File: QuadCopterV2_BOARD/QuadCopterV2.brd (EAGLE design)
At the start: 100 x 80 mm, 10 parts, among them IC1 EK-TM4C123GXLP, U1 GY-63MS5611, U2 GY-521MPU6050, U3 GY-63MS5611

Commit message: Eagle board design in process
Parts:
- removed U$1: SIM800L, SIM800L:SIP
- added U$7: SIM800L, SIM800L:SIP
- moved U1 277.7 mm to (-95.2, -166.4)
- moved U2 269.4 mm to (-95.2, -186.7)
- moved U$6 268.1 mm to (-85.1, -210.8)
- moved U$5 229.5 mm to (-104.1, -129.5)
- moved U3 228.9 mm to (-91.4, -143.5)
- moved U$3 196.5 mm to (-83.8, -105.4)
- moved U$2 162.0 mm to (-94.0, -39.4)
- moved U$4 113.8 mm to (-92.7, -71.1)
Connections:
- removed net N$27: U$1.3
- removed net N$28: U$1.4
- removed net N$30: U$1.7
- removed net N$31: U$1.5
- new net 5V1: U$2.D2
- new net N$1: U$7.3
- new net N$15: U$7.5
- new net N$6: U$7.4
- new net N$7: U$7.7
- net 5V0: now also U$7.1; no longer U$1.1, U$2.D2
- net GND: now also U$7.2, U$7.6; no longer U$1.2, U$1.6

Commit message: added modifications to eagle board, and to the mpu-6050 code
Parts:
- moved U$6 300.0 mm to (89.4, 33.2), turned to 90 degrees
- moved U2 293.4 mm to (36.8, 75.3), turned to 90 degrees
- moved U1 291.3 mm to (67.3, 75.3), turned to 90 degrees
- moved U$7 247.4 mm to (104.5, 103.0), turned to 225 degrees
- moved U$5 238.5 mm to (21.2, 73.3), turned to 135 degrees
- moved U3 217.6 mm to (74.1, -2.29), turned to 180 degrees
- moved U$2 197.2 mm to (101.5, -13.3), turned to 315 degrees
- moved U$3 162.7 mm to (1.19, 33.3), turned to 90 degrees
- moved IC1 132.9 mm to (51.5, 18.7)
- moved U$4 121.1 mm to (11.5, -9.49), turned to 135 degrees
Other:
- board size 100 x 80 mm -> 107.8 x 108.1 mm

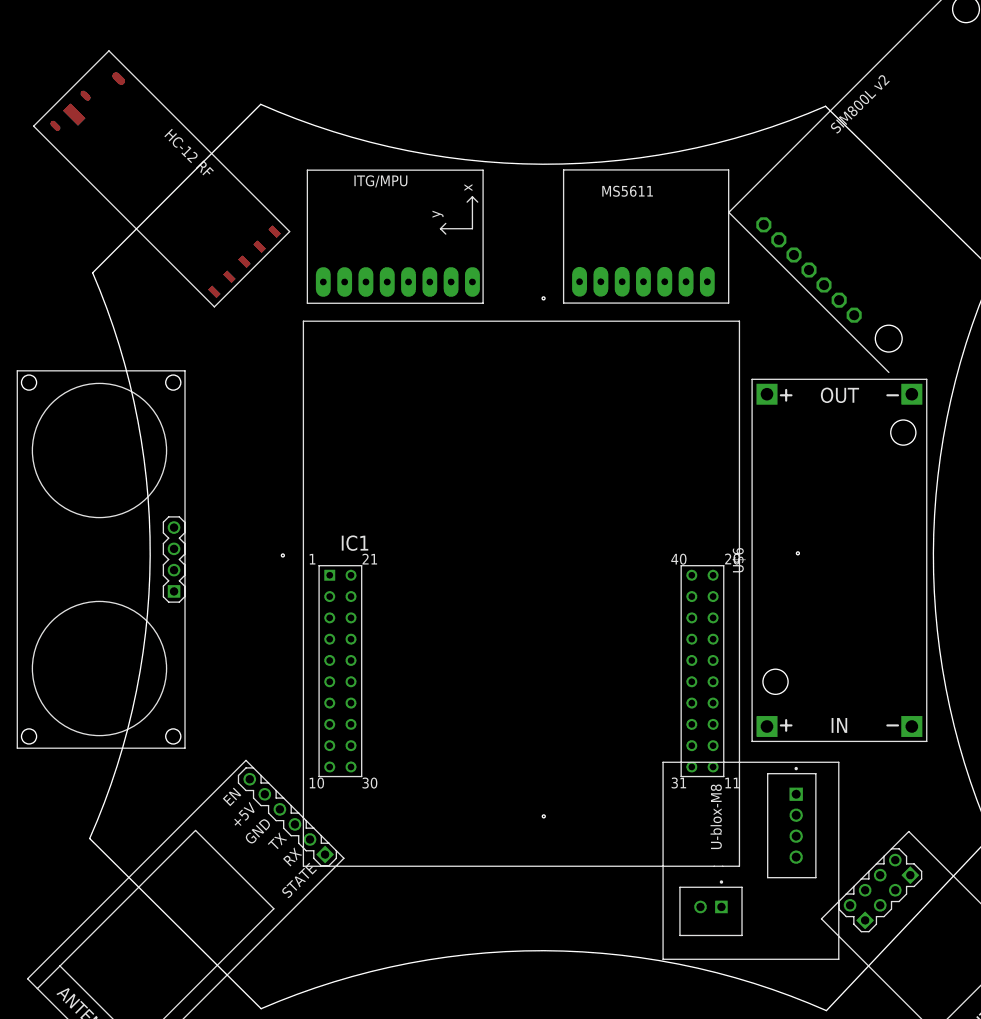
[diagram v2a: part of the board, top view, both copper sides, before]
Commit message: mpu-6050 finished, added more board eagle files, added altimeter code
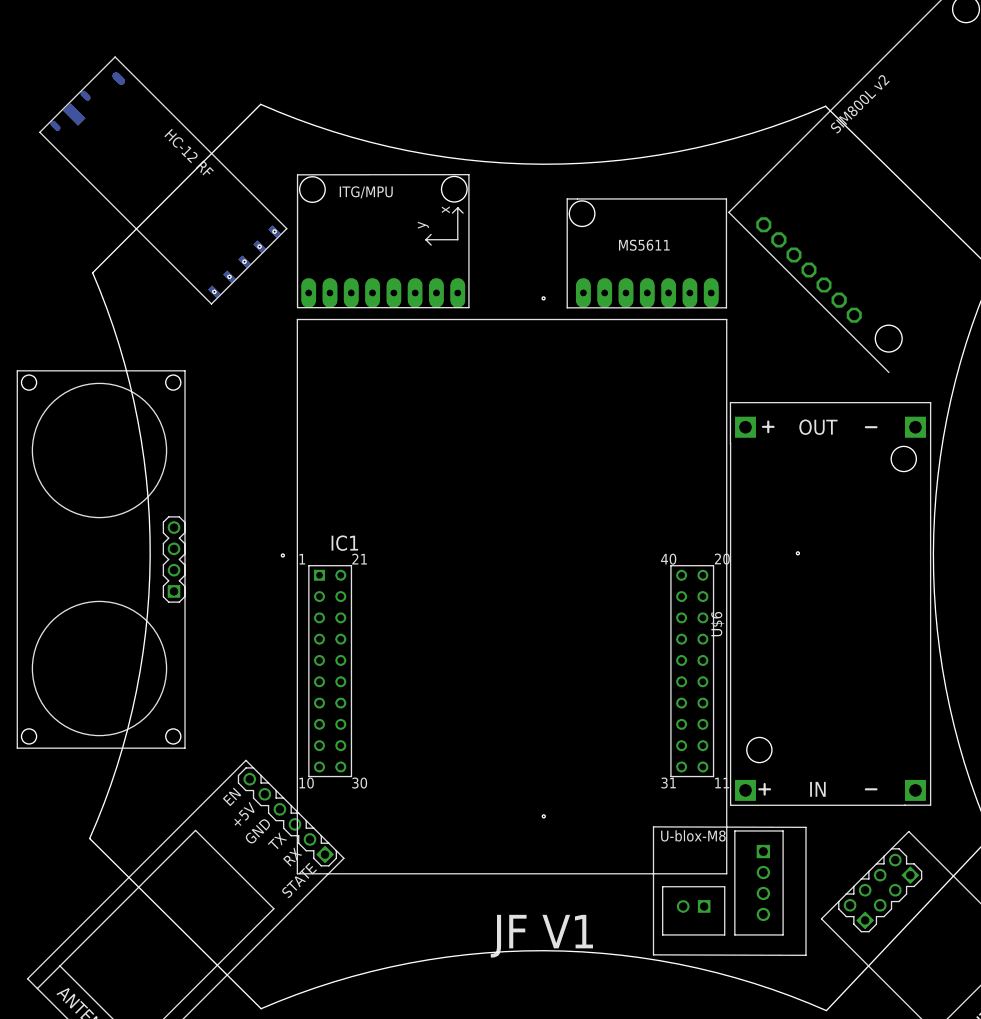
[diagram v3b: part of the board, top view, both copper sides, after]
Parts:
- moved U$6 8.04 mm to (86.9, 25.6)
- moved U3 7.87 mm to (70.2, -9.12)
- moved U2 2.18 mm to (35.0, 74.0)
- moved U1 1.41 mm to (67.8, 74.0)
- moved IC1 1.22 mm to (50.3, 18.7)
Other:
- board text added: "JF V1"
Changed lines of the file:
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@@
 <setting verticaltext="up"/>
 </settings>
-<grid distance="1" unitdist="mil" unit="mil" style="lines" multiple="1" display="no" altdistance="5" altunitdist="mil" altunit="mil"/>
+<grid distance="0.001" unitdist="mm" unit="mm" style="lines" multiple="1" display="no" altdistance="5" altunitdist="mil" altunit="mil"/>
 <layers>
 <layer number="1" name="Top" color="4" fill="1" visible="yes" active="yes"/>
@@
 <hole x="23.0632" y="33.8074" drill="0.35"/>
 <hole x="84.4804" y="34.0614" drill="0.35"/>
+<text x="54.306" y="-11.048" size="4" layer="21" font="fixed" align="center">JF V1</text>
 </plain>
 <attributes>
@@
 </autorouter>
 <elements>
-<element name="IC1" library="EK-TM4C123GXL" package="TM4C123LAUNCHPAD" value="EK-TM4C123GXLP" x="51.5112" y="18.7452" smashed="yes">
-<attribute name="AVAILABILITY" value="Unavailable" x="132.7912" y="4.7752" size="1.778" layer="27" display="off"/>
-<attribute name="DESCRIPTION" value=" TM4C123G LaunchPad™ Tiva™ C ARM® Cortex®-M4F MCU 32-Bit Embedded Evaluation Board " x="132.7912" y="4.7752" size="1.778" layer="27" display="off"/>
-<attribute name="MF" value="Texas Instruments" x="132.7912" y="4.7752" size="1.778" layer="27" display="off"/>
-<attribute name="MP" value="EK-TM4C123GXL" x="132.7912" y="4.7752" size="1.778" layer="27" display="off"/>
-<attribute name="NAME" x="33.4534" y="36.1671" size="1.780340625" layer="25" ratio="10" rot="R180"/>
-<attribute name="PACKAGE" value="None" x="132.7912" y="4.7752" size="1.778" layer="27" display="off"/>
-<attribute name="PRICE" value="None" x="132.7912" y="4.7752" size="1.778" layer="27" display="off"/>
-<attribute name="VALUE" x="69.3157" y="34.3114" size="1.78045" layer="27" ratio="10"/>
+<element name="IC1" library="EK-TM4C123GXL" package="TM4C123LAUNCHPAD" value="EK-TM4C123GXLP" x="50.292" y="18.7452" smashed="yes">
+<attribute name="AVAILABILITY" value="Unavailable" x="131.572" y="4.7752" size="1.778" layer="27" display="off"/>
+<attribute name="DESCRIPTION" value=" TM4C123G LaunchPad™ Tiva™ C ARM® Cortex®-M4F MCU 32-Bit Embedded Evaluation Board " x="131.572" y="4.7752" size="1.778" layer="27" display="off"/>
+<attribute name="MF" value="Texas Instruments" x="131.572" y="4.7752" size="1.778" layer="27" display="off"/>
+<attribute name="MP" value="EK-TM4C123GXL" x="131.572" y="4.7752" size="1.778" layer="27" display="off"/>
+<attribute name="NAME" x="32.2342" y="36.1671" size="1.780340625" layer="25" ratio="10" rot="R180"/>
+<attribute name="PACKAGE" value="None" x="131.572" y="4.7752" size="1.778" layer="27" display="off"/>
+<attribute name="PRICE" value="None" x="131.572" y="4.7752" size="1.778" layer="27" display="off"/>
+<attribute name="VALUE" x="68.0965" y="34.3114" size="1.78045" layer="27" ratio="10"/>
 </element>
 <element name="U$7" library="SIM800L" package="SIP" value="SIM800L" x="104.530028125" y="103.006028125" smashed="yes" rot="R225"/>
@@
 </element>
 <element name="U$5" library="hc12_433mhz" package="HC-12_FOOTPRINT" value="HC-12_FOOTPRINT" x="21.1836" y="73.3298" smashed="yes" rot="R135"/>
-<element name="U3" library="u_block_M8" package="U-BLOX" value="GY-63MS5611" x="74.1172" y="-2.286" smashed="yes" rot="R180"/>
-<element name="U1" library="gy-63" package="GY-63" value="GY-63MS5611" x="67.3354" y="75.3364" smashed="yes" rot="R90"/>
-<element name="U2" library="gy-521" package="GY-521" value="GY-521MPU6050" x="36.7792" y="75.311" smashed="yes" rot="R90"/>
-<element name="U$6" library="diy-modules" package="DC-DC-STEP-DOWN-LM2596" value="DC-DC-STEP-DOWN-LM2596" x="89.4334" y="33.2232" smashed="yes" rot="R90">
-<attribute name="NAME" x="78.0034" y="33.2232" size="1.27" layer="25" rot="R90" align="bottom-center"/>
-<attribute name="VALUE" x="100.8634" y="33.2232" size="1.27" layer="27" rot="R90" align="top-center"/>
+<element name="U3" library="u_block_M8" package="U-BLOX" value="GY-63MS5611" x="70.2056" y="-9.1186" smashed="yes" rot="R180"/>
+<element name="U1" library="gy-63" package="GY-63" value="GY-63MS5611" x="67.7926" y="74" smashed="yes" rot="R90"/>
+<element name="U2" library="gy-521" package="GY-521" value="GY-521MPU6050" x="35.0314" y="74" smashed="yes" rot="R90"/>
+<element name="U$6" library="diy-modules" package="DC-DC-STEP-DOWN-LM2596" value="DC-DC-STEP-DOWN-LM2596" x="86.868" y="25.6032" smashed="yes" rot="R90">
+<attribute name="NAME" x="75.438" y="25.6032" size="1.27" layer="25" rot="R90" align="bottom-center"/>
+<attribute name="VALUE" x="98.298" y="25.6032" size="1.27" layer="27" rot="R90" align="top-center"/>
 </element>
 </elements>
@@
 <contactref element="U2" pad="VCC"/>
 <contactref element="U$6" pad="OUT+"/>
-<wire x1="80.7974" y1="53.0352" x2="91.19399375" y2="62.460525" width="0" layer="19" extent="1-1"/>
-<wire x1="84.2772" y1="-2.166" x2="80.7974" y2="53.0352" width="0" layer="19" extent="1-1"/>
-<wire x1="31.1912" y1="31.4452" x2="84.2772" y2="-2.166" width="0" layer="19" extent="1-1"/>
-<wire x1="14.89741875" y1="65.24756875" x2="31.1912" y2="31.4452" width="0" layer="19" extent="1-1"/>
-<wire x1="10.0838" y1="29.5148" x2="31.1912" y2="31.4452" width="0" layer="19" extent="1-1"/>
+<wire x1="78.232" y1="49.1032" x2="91.19399375" y2="62.460525" width="0" layer="19" extent="1-1"/>
+<wire x1="58.9026" y1="65.11" x2="78.232" y2="49.1032" width="0" layer="19" extent="1-1"/>
+<wire x1="26.1414" y1="65.11" x2="58.9026" y2="65.11" width="0" layer="19" extent="1-1"/>
+<wire x1="14.89741875" y1="65.24756875" x2="26.1414" y2="65.11" width="0" layer="19" extent="16-16"/>
+<wire x1="29.972" y1="31.4452" x2="26.1414" y2="65.11" width="0" layer="19" extent="1-1"/>
+<wire x1="10.0838" y1="29.5148" x2="29.972" y2="31.4452" width="0" layer="19" extent="1-1"/>
 <wire x1="20.91174375" y1="5.326846875" x2="10.0838" y2="29.5148" width="0" layer="19" extent="1-1"/>
-<wire x1="58.4454" y1="66.4464" x2="20.91174375" y2="5.326846875" width="0" layer="19" extent="1-1"/>
-<wire x1="27.8892" y1="66.421" x2="58.4454" y2="66.4464" width="0" layer="19" extent="1-1"/>
+<wire x1="80.3656" y1="-8.9986" x2="78.232" y2="49.1032" width="0" layer="19" extent="1-1"/>
 </signal>
 <signal name="3V3">
@@
 <contactref element="U2" pad="GND"/>
 <contactref element="U$6" pad="OUT-"/>
-<wire x1="89.397940625" y1="64.256575" x2="82.2137375" y2="71.44078125" width="0" layer="19" extent="1-1"/>
-<wire x1="98.0694" y1="53.0352" x2="89.397940625" y2="64.256575" width="0" layer="19" extent="1-1"/>
-<wire x1="84.2772" y1="5.334" x2="82.2137375" y2="71.44078125" width="0" layer="19" extent="1-1"/>
-<wire x1="31.1912" y1="28.9052" x2="84.2772" y2="5.334" width="0" layer="19" extent="1-1"/>
-<wire x1="10.0838" y1="37.1348" x2="31.1912" y2="28.9052" width="0" layer="19" extent="1-1"/>
-<wire x1="22.70779375" y1="3.53079375" x2="10.0838" y2="37.1348" width="0" layer="19" extent="1-1"/>
-<wire x1="60.9854" y1="66.4464" x2="22.70779375" y2="3.53079375" width="0" layer="19" extent="1-1"/>
-<wire x1="30.4292" y1="66.421" x2="60.9854" y2="66.4464" width="0" layer="19" extent="1-1"/>
-<wire x1="97.788325" y1="-2.74551875" x2="30.4292" y2="66.421" width="0" layer="19" extent="1-1"/>
-<wire x1="16.693471875" y1="67.04361875" x2="31.1912" y2="28.9052" width="0" layer="19" extent="1-1"/>
-<wire x1="0.08111875" y1="117.675328125" x2="16.693471875" y2="67.04361875" width="0" layer="19" extent="1-1"/>
-<wire x1="3.926190625" y1="102.753990625" x2="0.08111875" y2="117.675328125" width="0" layer="19" extent="1-1"/>
-<wire x1="0.334090625" y1="99.1618875" x2="3.926190625" y2="102.753990625" width="0" layer="19" extent="1-1"/>
+<wire x1="82.2137375" y1="71.44078125" x2="89.397940625" y2="64.256575" width="0" layer="19" extent="1-1"/>
+<wire x1="98.504" y1="49.1032" x2="89.397940625" y2="64.256575" width="0" layer="19" extent="1-1"/>
+<wire x1="61.4426" y1="65.11" x2="82.2137375" y2="71.44078125" width="0" layer="19" extent="1-1"/>
+<wire x1="28.6814" y1="65.11" x2="61.4426" y2="65.11" width="0" layer="19" extent="1-1"/>
+<wire x1="16.693471875" y1="67.04361875" x2="28.6814" y2="65.11" width="0" layer="19" extent="16-16"/>
+<wire x1="3.484715625" y1="90.675128125" x2="16.693471875" y2="67.04361875" width="0" layer="19" extent="16-16"/>
+<wire x1="-0.468009375" y1="88.631590625" x2="3.484715625" y2="90.675128125" width="0" layer="19" extent="16-16"/>
+<wire x1="-4.060109375" y1="85.0394875" x2="-0.468009375" y2="88.631590625" width="0" layer="19" extent="16-16"/>
+<wire x1="10.0838" y1="37.1348" x2="16.693471875" y2="67.04361875" width="0" layer="19" extent="16-16"/>
+<wire x1="29.972" y1="28.9052" x2="10.0838" y2="37.1348" width="0" layer="19" extent="1-1"/>
+<wire x1="22.70779375" y1="3.53079375" x2="29.972" y2="28.9052" width="0" layer="19" extent="1-1"/>
+<wire x1="97.889925" y1="-4.320315625" x2="98.504" y2="49.1032" width="0" layer="19" extent="1-1"/>
+<wire x1="80.3656" y1="-1.4986" x2="97.889925" y2="-4.320315625" width="0" layer="19" extent="1-1"/>
 </signal>
 <signal name="SPI_SCK_3">

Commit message: news modifications on designed board
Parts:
- added C1, C2, C3, C4, C5, C6: C4.7U-SMD, smd-rlc:C4.7U-SMD
- added R1, R2: RSMD, smd-resistor:RSMD
- added R3, R4, R5: RSMD, smd-rlc:RSMD
- added U$1: SIM800L, SIM800L:SIP
- added U10, U7, U8, U9: ESC-30AMS5611, ESC-HW30A:ESC-30A
- added U4, U5, U6: MCP1825S-3302E/DBP1, MCP1825S-3302E_DB:SOT230P700X180-4N#P1
- U$3: value ULTRASONIC-HC-SR04 -> ULTRASONIC-HC-SR04#P; device diy-modules:ULTRASONIC-HC-SR04 -> diy-modules:ULTRASONIC-HC-SR04#P
- U$7: value SIM800L -> XT60; device SIM800L:SIP -> XT60:XT60
- moved U$7 126.4 mm to (46.1, -9.11), turned to 0 degrees
- moved U$3 13.9 mm to (13.4, 39.9), turned to 270 degrees
- moved U3 1.00 mm to (70.2, -10.1)
- moved U1 0.77 mm to (67.0, 74.0)
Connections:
- net A0 renamed PE3
- net ENABLE_4 renamed PB3
- net PA_3 renamed PA3
- net PA_4 renamed PA4
- net SPI_MISO_3 renamed PD2
- net U7_RX renamed PE0
- removed net 5V1: U$2.D2
- removed net ENABLE_0: IC1.7
- removed net ENABLE_1: IC1.8
- removed net ENABLE_2: IC1.36
- removed net ENABLE_3: IC1.37
- removed net ENABLE_5: IC1.14
- removed net ENABLE_6: IC1.15
- removed net N$10: U3.SCL
- removed net N$11: U3.SDA
- removed net N$12: U$5.SET
- removed net N$13: U$5.TXD
- removed net N$14: U$5.RXD
- removed net N$15: U$7.5
- removed net N$19: U$2.A2
- removed net N$2: U$4.6
- removed net N$21: U$2.B2
- removed net N$23: U$2.C2
- removed net N$24: U$2.D1
- removed net N$3: U$4.3
- removed net N$33: U$3.2
- removed net N$38: U1.SCL
- removed net N$39: U1.SDA
- removed net N$4: U$4.2
- removed net N$43: U2.SCL
- removed net N$44: U2.SDA
- removed net N$5: U$4.1
- removed net N$6: U$7.4
- removed net N$7: U$7.7
- removed net N$8: U3.U_TX
- removed net N$9: U3.U_RX
- removed net PA_2: IC1.11
- removed net PB_2: IC1.19
- removed net SPI_CS_3: IC1.24
- removed net SPI_MOSI_3: IC1.26
- removed net SPI_SCK_3: IC1.23
- removed net U7_TX: IC1.27
- new net 3V3_ESP: C4.2, U$2.B2, U$2.D2, U4.1
- new net 3V3_HC12: C2.2, U$5.VCC, U6.1
- new net 3V3_MS5611: C6.2, U$1.VDD, U1.VCC, U5.1
- new net PA2: IC1.11, U$2.C2
- new net PA5: IC1.8, U$4.6
- new net PB2: IC1.19, U$1.RST
- new net PB4: IC1.7, U$4.1
- new net PB6: IC1.14, U9.PWM
- new net PB7: IC1.15, U10.PWM
- new net PD0: IC1.23, U7.PWM
- new net PD1: IC1.24, U8.PWM
- new net PD3: IC1.26, R3.1, R4.1
- new net PE1: IC1.27, U$3.TRIG
- new net U4_RX: IC1.37, U$1.TXD
- new net U4_TX: IC1.36, U$1.RXD
- net 5V0: now also C1.1, C3.2, C5.1, R5.2, U$1.5V, U$3.VCC, U4.3, U5.3, U6.3; no longer IC1.21, U$3.1, U$5.VCC, U$7.1, U1.VCC
- net GND: now also C1.2, C2.1, C3.1, C4.1, C5.2, C6.1, R2.1, R4.2, U$1.GND, U$1.PGND, U$3.GND, U10.GND, U4.2, U4.4, U5.2, U5.4, U6.2, U6.4, U7.GND, U8.GND, U9.GND; no longer U$3.4, U$5.GND1, U$5.GND2, U$5.MCHFIX, U$7.2, U$7.6
- net I2C_SCL_1: now also U1.SCL, U2.SCL, U3.SCL
- net I2C_SDA_1: now also U1.SDA, U2.SDA, U3.SDA
- net N$1: now also IC1.21, R5.1; no longer U$7.3
- net N$34: now also R1.1, U$3.ECHO; no longer U$3.3
- net PB5: now also U$5.SET
- net PE2: now also R1.2, R2.2
- net U1_RX: now also U$5.TXD
- net U1_TX: now also U$5.RXD
- net U2_RX: now also U3.U_TX
- net U2_TX: now also U3.U_RX
- net U3_RX: now also U$2.A2
- net U3_TX: now also U$2.D1
- net U5_RX: now also U$4.3
- net U5_TX: now also U$4.2
- net VBAT+: now also R3.2, U$7.+
- net VBAT-: now also U$7.-
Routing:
- net GND: track 0.00 -> 475.5 mm, vias 0 -> 6
- net 5V0: track 0.00 -> 310.8 mm, vias 0 -> 4
- net I2C_SDA_1: track 0.00 -> 214.0 mm, vias 0 -> 2
- net I2C_SCL_1: track 0.00 -> 199.2 mm, vias 0 -> 2
- net PB6: track 0.00 -> 120.8 mm, vias 0 -> 2
- net PB7: track 0.00 -> 119.2 mm, vias 0 -> 2
- net N$34: track 0.00 -> 106.8 mm, vias 0 -> 2
- net PD0: track 0.00 -> 101.1 mm, vias 0 -> 2
- net PD1: track 0.00 -> 87.5 mm, vias 0 -> 2
- net VBAT+: track 0.00 -> 72.5 mm, vias 0 -> 2
- net U4_TX: track 0.00 -> 71.0 mm, vias 0 -> 2
- net PA5: track 0.00 -> 67.4 mm, vias 0 -> 2
- net VBAT-: track 0.00 -> 67.2 mm
- net PA2: track 0.00 -> 65.5 mm, vias 0 -> 2
- net U4_RX: track 0.00 -> 63.8 mm, vias 0 -> 2
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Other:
- board size 107.8 x 108.1 mm -> 108.1 x 108.1 mm
- board text added: "03/2020"

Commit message: final version of quadcopter board
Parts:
- removed R5: RSMD, smd-rlc:RSMD
- added R6: RSMD, smd-rlc:RSMD
- R1: value RSMD -> 1k7; device smd-resistor:RSMD -> smd-rlc:RSMD
- R2: value RSMD -> 3K3; device smd-resistor:RSMD -> smd-rlc:RSMD
- R3: value RSMD -> 11k7
- R4: value RSMD -> 3k3
- moved R2 0.76 mm to (49.0, 23.0)
- moved R1 0.67 mm to (51.0, 20.0)
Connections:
- removed net GND2: IC1.20
- removed net N$17: U$5.ANT
- net 5V0: now also R6.2; no longer R5.2
- net GND: now also IC1.20
- net N$1: now also R6.1; no longer R5.1
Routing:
- net 5V0: track 310.8 -> 314.0 mm
- net N$1: track 3.70 -> 4.89 mm
- net GND: track 475.5 -> 476.2 mm
- net N$34: track 106.8 -> 106.2 mm
- net U1_RX: track 53.0 -> 53.6 mm
- added copper zone on layer 16, net GND
